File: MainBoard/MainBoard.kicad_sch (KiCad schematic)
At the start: 51 parts, among them J1 Conn_02x37_Counter_Clockwise, J2 Conn_02x37_Counter_Clockwise, J3 Conn_01x04_Pin, J4 SER1, J5 SER1, J6 JST, J7 UART, Q1 2N3904, Q2 2N3904, Q3 2N3904, Q4 2N3904, Q5 2N3904, Q6 2N3904, U2 TMAG5273A1QDBVR

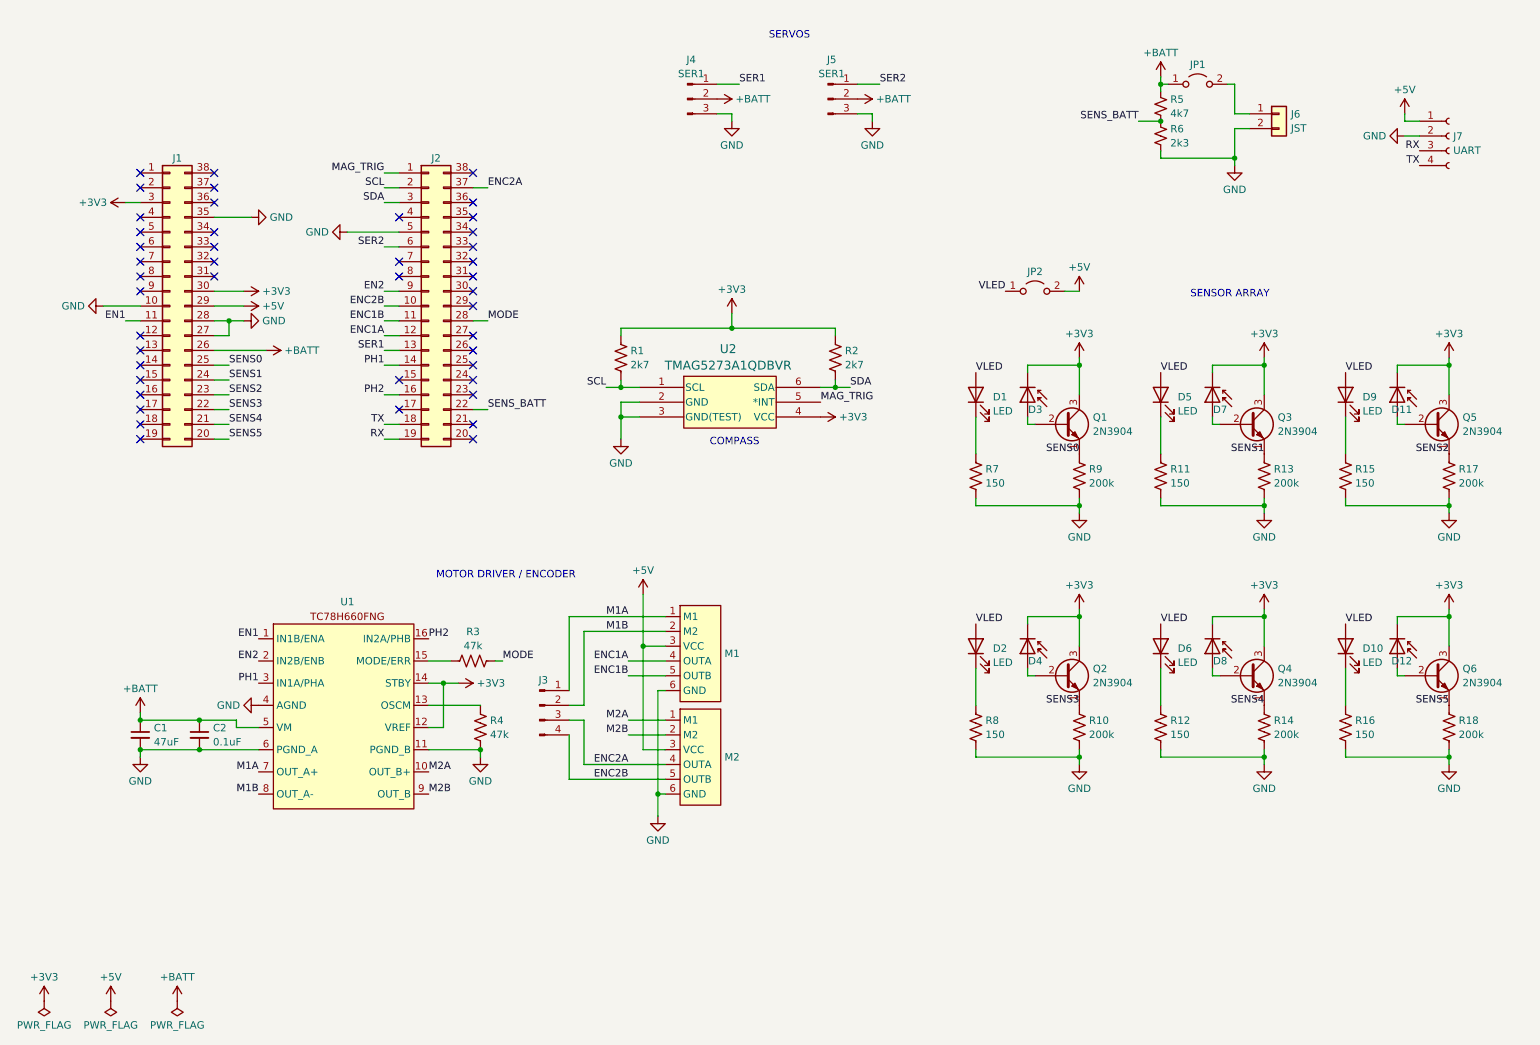
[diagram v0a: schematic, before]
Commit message: add external 5V regulator
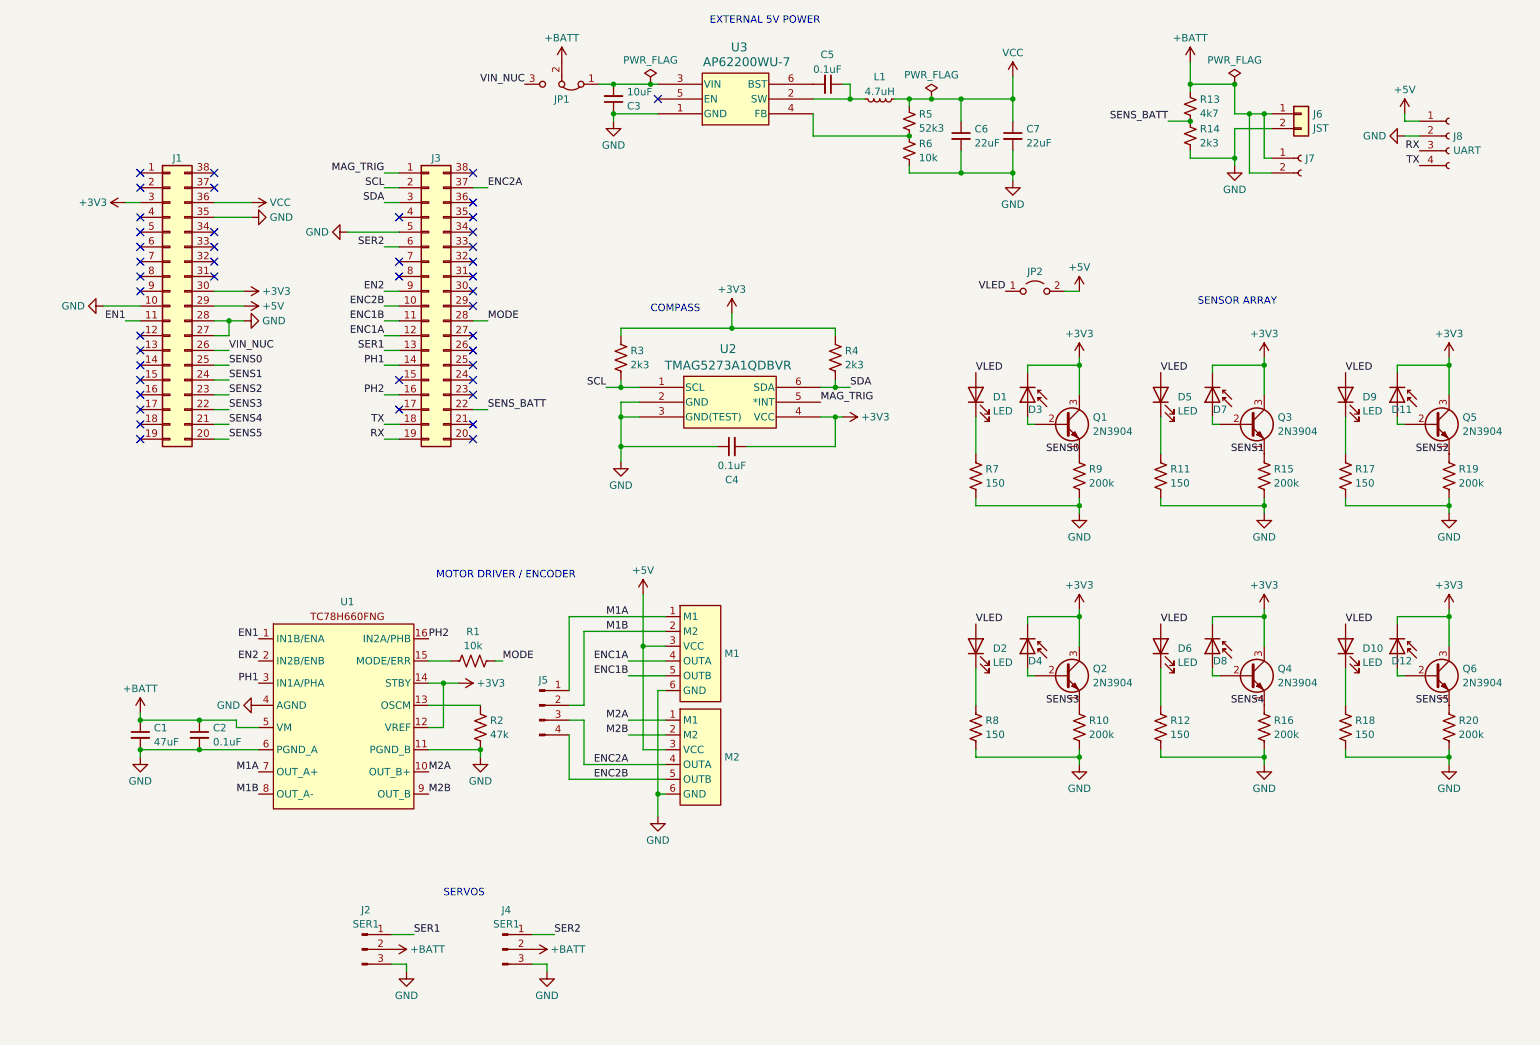
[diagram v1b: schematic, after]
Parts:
- removed JP1: Jumper_2_Open, symbol Jumper:Jumper_2_Open
- added C3: 10uF, symbol Device:C_Small
- added C4, C5: 0.1uF, symbol Device:C_Small
- added C6, C7: 22uF, symbol Device:C_Small
- added J7: Conn_01x02_Socket, symbol Connector:Conn_01x02_Socket
- added JP1: Jumper_3_Bridged12, symbol Jumper:Jumper_3_Bridged12
- added L1: 4.7uH, symbol Device:L_Small
- added R5: 52k3, symbol Device:R_Small_US
- added R6: 10k, symbol Device:R_Small_US
- added U3: AP62200WU-7, TSOT26-WU_DIO, symbol AP62200WU_7:AP62200WU-7
- R1: renamed from R3; value 47k -> 10k
- R3: renamed from R1; value 2k7 -> 2k3
- R4: renamed from R2; value 2k7 -> 2k3
- renumbered J4 to J2, J2 to J3, J5 to J4, J3 to J5, J7 to J8, R5 to R13, R6 to R14, R13 to R15, R14 to R16, R15 to R17, R16 to R18, R17 to R19, R4 to R2, R18 to R20
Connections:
- net +3V3: now also C4.2
- net +BATT: now also J6.1 (Pin_1), J7.1 (Pin_1), J7.2 (Pin_2), JP1.2 (C); no longer J1.26 (Pin_26)
- net GND: now also C3.1, C4.1, C6.2, C7.2, R6.2, U3.1 (GND)
- net VCC: now reaches J1.36 (Pin_36)
- net VCC: now also C6.1, C7.1, L1.2, R5.1
- new net: C3.2, JP1.1 (A), U3.3 (VIN)
- new net: R5.2, R6.1, U3.4 (FB)
- new net: C5.1, L1.1, U3.2 (SW)
- new net: C5.2, U3.6 (BST)
- new net VIN_NUC: J1.26 (Pin_26), JP1.3 (B)
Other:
- note added: "EXTERNAL 5V POWER"
- moved on the sheet: J2, J4, J6, R13, R14

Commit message: mainboard layout
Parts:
- added J9: Conn_01x05_Socket, Connector_PinHeader_2.54mm:PinHeader_1x05_P2.54mm_Vertical, symbol Connector:Conn_01x05_Socket
- added JP3: SolderJumper_3_Bridged12, Jumper:SolderJumper-3_P2.0mm_Open_TrianglePad1.0x1.5mm, symbol Jumper:SolderJumper_3_Open
- C1: footprint (none) -> Capacitor_THT:C_Radial_D5.0mm_H7.0mm_P2.00mm
- C2, C3, C4, C5, C6, C7: footprint (none) -> Capacitor_SMD:C_0805_2012Metric_Pad1.18x1.45mm_HandSolder
- D1, D10, D2, D5, D6, D9: footprint (none) -> LED_THT:LED_D3.0mm
- D11, D12, D3, D4, D7, D8: footprint (none) -> LED_THT:LED_D5.0mm
- J1, J3: value Conn_02x37_Counter_Clockwise -> Conn_02x19_Odd_Even; footprint (none) -> Connector_PinSocket_2.54mm:PinSocket_2x19_P2.54mm_Vertical; symbol Connector_Generic:Conn_02x19_Counter_Clockwise -> Connector_Generic:Conn_02x19_Odd_Even
- J2, JP1: footprint (none) -> Connector_PinHeader_2.54mm:PinHeader_1x03_P2.54mm_Vertical
- J4: value SER1 -> SER2; footprint (none) -> Connector_PinHeader_2.54mm:PinHeader_1x03_P2.54mm_Vertical
- J5: footprint (none) -> Connector_PinHeader_2.54mm:PinHeader_1x04_P2.54mm_Horizontal
- J6: footprint (none) -> Connector_JST:JST_PH_S2B-PH-K_1x02_P2.00mm_Horizontal
- J7: footprint (none) -> Connector_PinSocket_2.54mm:PinSocket_1x02_P2.54mm_Vertical
- J8: footprint (none) -> Connector_PinSocket_2.54mm:PinSocket_1x04_P2.54mm_Vertical
- JP2: footprint (none) -> Connector_PinHeader_2.54mm:PinHeader_1x02_P2.54mm_Vertical
- L1: footprint (none) -> Inductor_SMD:L_0805_2012Metric_Pad1.15x1.40mm_HandSolder
- M1, M2: footprint (none) -> MainBoard:N20
- Q1, Q2, Q3, Q4, Q5, Q6: value 2N3904 -> MMBT3904; footprint Package_TO_SOT_THT:TO-92_Inline -> Package_TO_SOT_SMD:SOT-23_Handsoldering; symbol Transistor_BJT:2N3904 -> Transistor_BJT:MMBT3904
- R1, R10, R11, R12, R13, R15, R16, R17, R18, R19, R2, R20, R5, R6, R7, R8, R9: footprint (none) -> Resistor_SMD:R_0805_2012Metric_Pad1.20x1.40mm_HandSolder
- R14, R3, R4: value 2k3 -> 2k2; footprint (none) -> Resistor_SMD:R_0805_2012Metric_Pad1.20x1.40mm_HandSolder
- U1: footprint (none) -> Package_SO:TSSOP-16_4.4x5mm_P0.65mm
- U2: footprint SOT23-6_DBV_TEX -> Package_TO_SOT_SMD:TSOT-23-6_HandSoldering
- U3: footprint TSOT26-WU_DIO -> Package_TO_SOT_SMD:TSOT-23-6_HandSoldering
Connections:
- net +3V3: now also J1.17 (Pin_17), J1.6 (Pin_6), J9.1 (Pin_1), JP3.1 (A); no longer J1.3 (Pin_3), J1.30 (Pin_30), U1.14 (STBY)
- net +5V: now also J1.19 (Pin_19); no longer J1.29 (Pin_29)
- net +BATT: no longer J7.2 (Pin_2)
- net EN1: now also J1.22 (Pin_22); no longer J1.11 (Pin_11)
- net EN2: now also J3.18 (Pin_18); no longer J3.9 (Pin_9)
- net ENC1A: now also J3.24 (Pin_24); no longer J3.12 (Pin_12)
- net ENC1B: now also J3.22 (Pin_22); no longer J3.11 (Pin_11)
- net ENC2A: now also J3.3 (Pin_3); no longer J3.37 (Pin_37)
- net ENC2B: now also J3.20 (Pin_20); no longer J3.10 (Pin_10)
- net GND: now also J1.20 (Pin_20), J1.21 (Pin_21), J1.23 (Pin_23), J1.7 (Pin_7), J3.10 (Pin_10), J7.2 (Pin_2), J9.5 (Pin_5), JP3.3 (B); no longer J1.10 (Pin_10), J1.27 (Pin_27), J1.28 (Pin_28), J1.35 (Pin_35), J3.5 (Pin_5)
- net MAG_TRIG: now also J3.2 (Pin_2), J9.2 (Pin_2); no longer J3.1 (Pin_1)
- net MODE: now also J3.21 (Pin_21); no longer J3.28 (Pin_28)
- net PH1: now also J3.28 (Pin_28); no longer J3.14 (Pin_14)
- net PH2: now also J3.32 (Pin_32); no longer J3.16 (Pin_16)
- net RX: now also J3.38 (Pin_38); no longer J3.19 (Pin_19)
- net SCL: now also J3.4 (Pin_4), J9.4 (Pin_4); no longer J3.2 (Pin_2)
- net SDA: now also J3.6 (Pin_6), J9.3 (Pin_3); no longer J3.3 (Pin_3)
- net SENS0: now also J1.27 (Pin_27), Q1.2 (E); no longer J1.25 (Pin_25), Q1.1 (E)
- net SENS1: now also J1.29 (Pin_29), Q3.2 (E); no longer J1.24 (Pin_24), Q3.1 (E)
- net SENS2: now also J1.31 (Pin_31), Q5.2 (E); no longer J1.23 (Pin_23), Q5.1 (E)
- net SENS3: now also J1.33 (Pin_33), Q2.2 (E); no longer J1.22 (Pin_22), Q2.1 (E)
- net SENS4: now also J1.35 (Pin_35), Q4.2 (E); no longer J1.21 (Pin_21), Q4.1 (E)
- net SENS5: now also J1.37 (Pin_37), Q6.2 (E); no longer J1.20 (Pin_20), Q6.1 (E)
- net SENS_BATT: now also J3.33 (Pin_33); no longer J3.22 (Pin_22)
- net SER1: now also J3.26 (Pin_26); no longer J3.13 (Pin_13)
- net SER2: now also J3.12 (Pin_12); no longer J3.6 (Pin_6)
- net TX: now also J3.36 (Pin_36); no longer J3.18 (Pin_18)
- net VCC: now also J1.5 (Pin_5); no longer J1.36 (Pin_36)
- net VIN_NUC: now also J1.25 (Pin_25); no longer J1.26 (Pin_26)
- net at D3.2 (A): now also Q1.1 (B); no longer Q1.2 (B)
- net at D7.2 (A): now also Q3.1 (B); no longer Q3.2 (B)
- net at D8.2 (A): now also Q4.1 (B); no longer Q4.2 (B)
- net at D4.2 (A): now also Q2.1 (B); no longer Q2.2 (B)
- net at D11.2 (A): now also Q5.1 (B); no longer Q5.2 (B)
- net at D12.2 (A): now also Q6.1 (B); no longer Q6.2 (B)
- new net: JP3.2 (C), U1.14 (STBY)
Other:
- moved on the sheet: C1, C2, C4, J1, J3, R1, R2, R3, R4, U1, U2

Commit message: routing
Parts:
- J6: footprint Connector_JST:JST_PH_S2B-PH-K_1x02_P2.00mm_Horizontal -> Connector_JST:JST_PH_B2B-PH-K_1x02_P2.00mm_Vertical
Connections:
- net +3V3: no longer J1.6 (Pin_6)
- net ENC2A: no longer J5.3 (Pin_3)
- net ENC2B: no longer J5.4 (Pin_4)
- net M2A: now also J5.3 (Pin_3)
- net M2B: now also J5.4 (Pin_4)
- net SENS1: now also Q2.2 (E), R10.1; no longer Q3.2 (E), R15.1
- net SENS2: now also Q3.2 (E), R15.1; no longer Q5.2 (E), R19.1
- net SENS3: now also Q4.2 (E), R16.1; no longer Q2.2 (E), R10.1
- net SENS4: now also Q5.2 (E), R19.1; no longer Q4.2 (E), R16.1
- no-connect marks 44 -> 45
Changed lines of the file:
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@@
   (no_connect (at 90.17 71.12))
   (no_connect (at 33.02 63.5))
+  (no_connect (at 33.02 53.34))
   (no_connect (at 77.47 66.04))
   (wire (pts (xy 214.63 148.59) (xy 214.63 147.32))
@@
     (stroke (width 0) (type default))
   )
-  (wire (pts (xy 123.19 142.24) (xy 129.54 142.24))
-    (stroke (width 0) (type default))
-  )
   (wire (pts (xy 85.09 185.42) (xy 85.09 184.15))
     (stroke (width 0) (type default))
@@
     (stroke (width 0) (type default))
   )
-  (wire (pts (xy 113.03 152.4) (xy 129.54 152.4))
-    (stroke (width 0) (type default))
-  )
   (wire (pts (xy 166.37 87.63) (xy 167.64 87.63))
     (stroke (width 0) (type default))
@@
     (stroke (width 0) (type default))
   )
-  (wire (pts (xy 113.03 144.78) (xy 113.03 152.4))
-    (stroke (width 0) (type default))
-  )
   (wire (pts (xy 146.05 81.28) (xy 148.59 81.28))
     (stroke (width 0) (type default))
@@
     (stroke (width 0) (type default))
   )
-  (wire (pts (xy 113.03 142.24) (xy 115.57 142.24))
+  (wire (pts (xy 113.03 142.24) (xy 129.54 142.24))
     (stroke (width 0) (type default))
   )
@@
     (stroke (width 0) (type default))
   )
+  (wire (pts (xy 113.03 144.78) (xy 129.54 144.78))
+    (stroke (width 0) (type default))
+  )
   (wire (pts (xy 120.65 38.1) (xy 120.65 39.37))
     (stroke (width 0) (type default))
@@
     (stroke (width 0) (type default))
   )
-  (wire (pts (xy 123.19 144.78) (xy 129.54 144.78))
-    (stroke (width 0) (type default))
-  )
   (wire (pts (xy 74.93 60.96) (xy 77.47 60.96))
     (stroke (width 0) (type default))
@@
     (stroke (width 0) (type default))
   )
+  (wire (pts (xy 123.19 152.4) (xy 129.54 152.4))
+    (stroke (width 0) (type default))
+  )
   (wire (pts (xy 223.52 81.28) (xy 223.52 82.55))
     (stroke (width 0) (type default))
@@
     (stroke (width 0) (type default))
   )
+  (wire (pts (xy 123.19 149.86) (xy 129.54 149.86))
+    (stroke (width 0) (type default))
+  )
   (wire (pts (xy 128.27 154.94) (xy 129.54 154.94))
     (stroke (width 0) (type default))
@@
     (stroke (width 0) (type default))
   )
-  (wire (pts (xy 115.57 142.24) (xy 115.57 149.86))
-    (stroke (width 0) (type default))
-  )
   (wire (pts (xy 214.63 105.41) (xy 214.63 104.14))
     (stroke (width 0) (type default))
@@
     (stroke (width 0) (type default))
   )
-  (wire (pts (xy 30.48 53.34) (xy 33.02 53.34))
-    (stroke (width 0) (type default))
-  )
   (wire (pts (xy 182.88 105.41) (xy 182.88 104.14))
     (stroke (width 0) (type default))
@@
   )
   (wire (pts (xy 146.05 72.39) (xy 146.05 71.12))
-    (stroke (width 0) (type default))
-  )
-  (wire (pts (xy 115.57 149.86) (xy 129.54 149.86))
     (stroke (width 0) (type default))
   )
@@
     (effects (font (size 1.27 1.27)) (justify right bottom))
   )
-  (label "SENS1" (at 232.41 96.52 180) (fields_autoplaced)
+  (label "SENS1" (at 200.66 139.7 180) (fields_autoplaced)
     (effects (font (size 1.27 1.27)) (justify right bottom))
   )
@@
     (effects (font (size 1.27 1.27)) (justify left bottom))
   )
-  (label "SENS3" (at 200.66 139.7 180) (fields_autoplaced)
+  (label "SENS3" (at 232.41 139.7 180) (fields_autoplaced)
     (effects (font (size 1.27 1.27)) (justify right bottom))
   )
@@
     (effects (font (size 1.27 1.27)) (justify right bottom))
   )
-  (label "SENS4" (at 232.41 139.7 180) (fields_autoplaced)
+  (label "SENS4" (at 264.16 96.52 180) (fields_autoplaced)
     (effects (font (size 1.27 1.27)) (justify right bottom))
   )
@@
     (effects (font (size 1.27 1.27)) (justify left bottom))
   )
-  (label "SENS2" (at 264.16 96.52 180) (fields_autoplaced)
+  (label "SENS2" (at 232.41 96.52 180) (fields_autoplaced)
     (effects (font (size 1.27 1.27)) (justify right bottom))
   )
@@
     )
   )
-  (symbol (lib_id "power:+BATT") (at 111.76 29.21 0) (mirror y) (unit 1)
-    (in_bom yes) (on_board yes) (dnp no) (fields_autoplaced)
+  (symbol (lib_id "power:+BATT") (at 111.76 29.21 0) (unit 1)
+    (in_bom yes) (on_board yes) (dnp no)
     (property "Reference" "#PWR021" (at 111.76 33.02 0)
       (effects (font (size 1.27 1.27)) hide)
@@
         (path "/4e7ed763-87f3-45bc-a98b-73c8bb560891"
           (reference "U2") (unit 1)
-        )
-      )
-    )
-  )
-  (symbol (lib_id "power:+3V3") (at 30.48 53.34 90) (unit 1)
-    (in_bom yes) (on_board yes) (dnp no) (fields_autoplaced)
-    (property "Reference" "#PWR04" (at 34.29 53.34 0)
-      (effects (font (size 1.27 1.27)) hide)
-    )
-    (property "Value" "+3V3" (at 27.305 53.34 90)
-      (effects (font (size 1.27 1.27)) (justify left))
-    )
-    (property "Footprint" "" (at 30.48 53.34 0)
-      (effects (font (size 1.27 1.27)) hide)
-    )
-    (property "Datasheet" "" (at 30.48 53.34 0)
-      (effects (font (size 1.27 1.27)) hide)
-    )
-    (pin "1")
-    (instances
-      (project "MainBoard"
-        (path "/4e7ed763-87f3-45bc-a98b-73c8bb560891"
-          (reference "#PWR04") (unit 1)
         )
       )
@@
       (effects (font (size 1.27 1.27)) (justify left))
     )
-    (property "Footprint" "Connector_JST:JST_PH_S2B-PH-K_1x02_P2.00mm_Horizontal" (at 238.76 38.1 0)
-      (effects (font (size 1.27 1.27)) hide)
-    )
+    (property "Footprint" "Connector_JST:JST_PH_B2B-PH-K_1x02_P2.00mm_Vertical" (at 238.76 38.1 0)
+      (effects (font (size 1.27 1.27)) hide)
+    )

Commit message: update routing
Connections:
- net GND: now also J3.31 (Pin_31)
- no-connect marks 45 -> 44
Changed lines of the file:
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@@
   (no_connect (at 33.02 60.96))
   (no_connect (at 90.17 78.74))
-  (no_connect (at 90.17 86.36))
   (no_connect (at 33.02 86.36))
   (no_connect (at 90.17 83.82))
@@
     (stroke (width 0) (type default))
   )
+  (wire (pts (xy 91.44 86.36) (xy 90.17 86.36))
+    (stroke (width 0) (type default))
+  )
   (wire (pts (xy 223.52 91.44) (xy 224.79 91.44))
     (stroke (width 0) (type default))
@@
     (stroke (width 0) (type default))
   )
+  (wire (pts (xy 91.44 85.09) (xy 92.71 85.09))
+    (stroke (width 0) (type default))
+  )
   (wire (pts (xy 171.45 35.56) (xy 175.26 35.56))
     (stroke (width 0) (type default))
@@
     (stroke (width 0) (type default))
   )
+  (wire (pts (xy 91.44 85.09) (xy 91.44 86.36))
+    (stroke (width 0) (type default))
+  )
   (wire (pts (xy 120.65 38.1) (xy 120.65 39.37))
     (stroke (width 0) (type default))
@@
         )
       )
+    )
+  )
+  (symbol (lib_id "power:GND") (at 92.71 85.09 90) (unit 1)
+    (in_bom yes) (on_board yes) (dnp no) (fields_autoplaced)
+    (property "Reference" "#PWR04" (at 99.06 85.09 0)
+      (effects (font (size 1.27 1.27)) hide)
+    )
+    (property "Value" "GND" (at 95.885 85.09 90)
+      (effects (font (size 1.27 1.27)) (justify right))
+    )
+    (property "Footprint" "" (at 92.71 85.09 0)
+      (effects (font (size 1.27 1.27)) hide)
+    )
+    (property "Datasheet" "" (at 92.71 85.09 0)
+      (effects (font (size 1.27 1.27)) hide)
+    )
+    (pin "1")
+    (instances
+      (project "MainBoard"
+        (path "/4e7ed763-87f3-45bc-a98b-73c8bb560891"
+          (reference "#PWR04") (unit 1)
+        )
+      )

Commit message: update routing
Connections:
- net +3V3: now also J1.15 (Pin_15); no longer J1.17 (Pin_17)
- net +5V: now also J1.17 (Pin_17); no longer J1.19 (Pin_19)
- net GND: now also J1.19 (Pin_19); no longer J1.23 (Pin_23)
- net VIN_NUC: now also J1.23 (Pin_23); no longer J1.25 (Pin_25)
